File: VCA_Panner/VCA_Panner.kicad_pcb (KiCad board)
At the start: 2 copper layers, 43 x 110 mm, 70 parts, among them J1 CV1, J2 CV2, J3 Ch1_in, J4 Ch1_out, J6 Ch2_in, J7 Ch2_out, U1 TL074, U2 TL074, U3 TL074, U5 AS3360

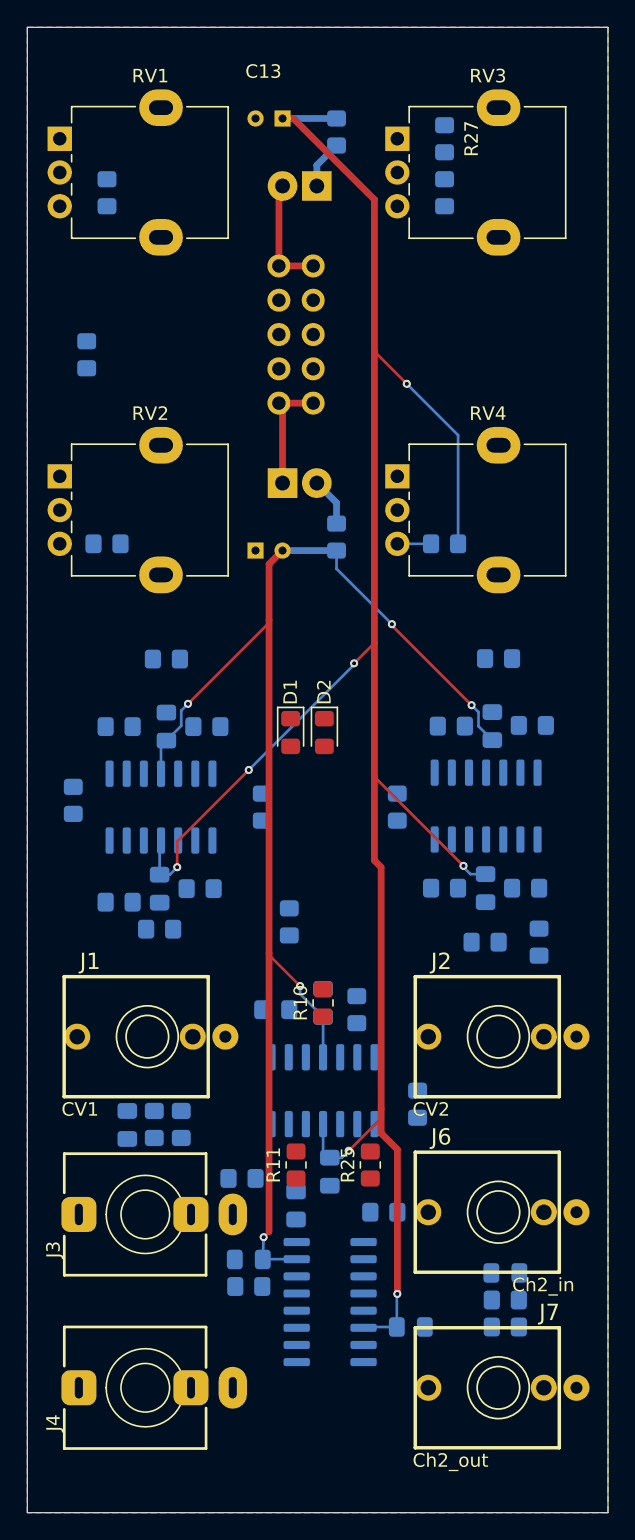
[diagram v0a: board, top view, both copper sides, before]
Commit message: vca_panner led added, routing started
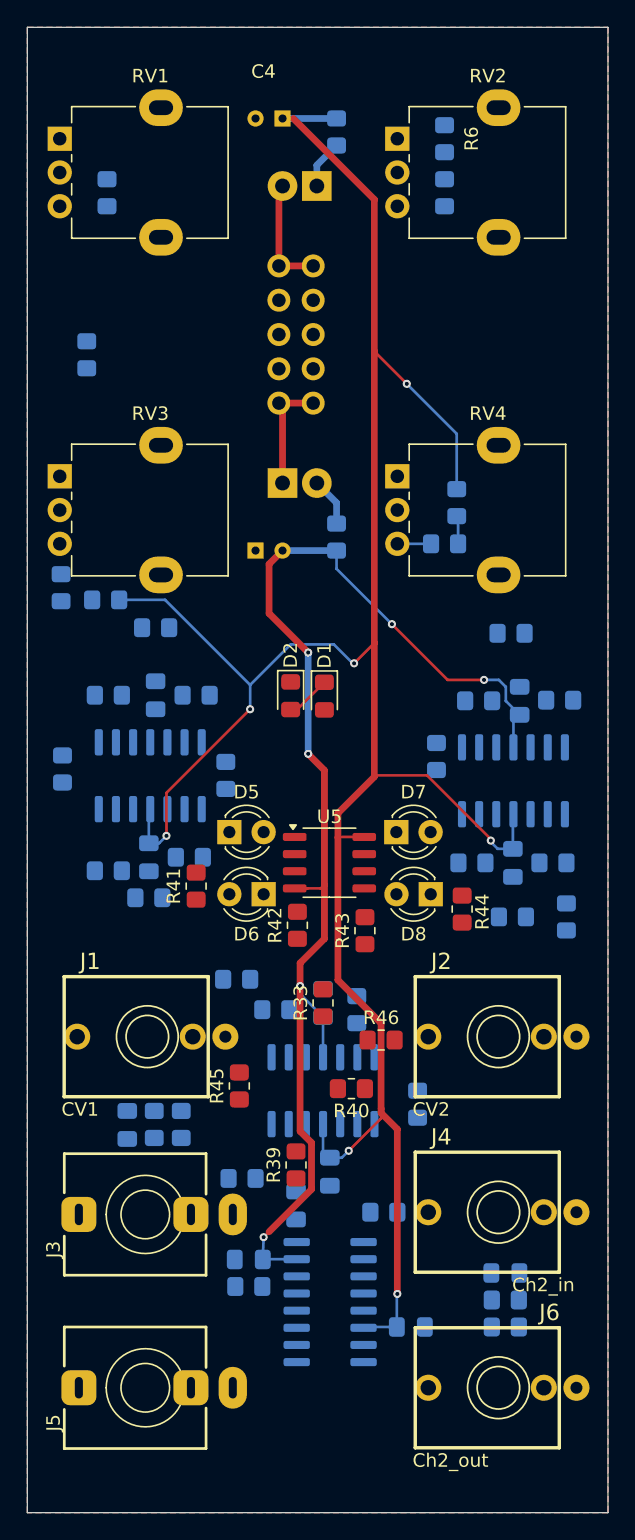
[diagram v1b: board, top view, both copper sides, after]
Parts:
- removed the R14 at (113.0, 95.5)
- added D5: LED, LED_THT:LED_D3.0mm, F.Cu at (122.1, 116.8)
- added D6: LED, LED_THT:LED_D3.0mm, F.Cu at (124.6, 121.5)
- added D7: LED, LED_THT:LED_D3.0mm, F.Cu at (134.4, 116.8)
- added D8: LED, LED_THT:LED_D3.0mm, F.Cu at (137.0, 121.5)
- added R23: 330k, Resistor_SMD:R_0805_2012Metric_Pad1.20x1.40mm_HandSolder, B.Cu at (109.6, 98.8)
- added R24: 400k, Resistor_SMD:R_0805_2012Metric_Pad1.20x1.40mm_HandSolder, B.Cu at (112.9, 99.7)
- added R26: 400k, Resistor_SMD:R_0805_2012Metric_Pad1.20x1.40mm_HandSolder, B.Cu at (138.9, 92.5)
- added R41: 1M, Resistor_SMD:R_0805_2012Metric_Pad1.20x1.40mm_HandSolder, F.Cu at (119.6, 120.8)
- added R42: 1.5k, Resistor_SMD:R_0805_2012Metric_Pad1.20x1.40mm_HandSolder, F.Cu at (127.1, 123.8)
- added R43: 1M, Resistor_SMD:R_0805_2012Metric_Pad1.20x1.40mm_HandSolder, F.Cu at (132.1, 124.2)
- added R44: 1.5k, Resistor_SMD:R_0805_2012Metric_Pad1.20x1.40mm_HandSolder, F.Cu at (139.3, 122.5)
- added R45: 1M, Resistor_SMD:R_0805_2012Metric_Pad1.20x1.40mm_HandSolder, F.Cu at (122.8, 135.7)
- added R46: 1M, Resistor_SMD:R_0805_2012Metric_Pad1.20x1.40mm_HandSolder, F.Cu at (133.3, 132.2)
- added U5: LM358, Package_SO:SO-8_3.9x4.9mm_P1.27mm, F.Cu at (129.5, 119.1)
- R25: renamed from R28; value 730k -> 330k
- moved R40 5.82 mm to (131.1, 135.8), turned to 180 degrees
- moved R34 5.77 mm to (122.6, 127.8), turned to 180 degrees
- moved R22 4.74 mm to (137.4, 111.2)
- moved R4 3.58 mm to (121.8, 112.7)
- moved C7 2.76 mm to (143.6, 107.1)
- moved C8 2.76 mm to (143.1, 119.1)
- moved R10 2.76 mm to (147.0, 123.1)
- moved R12 2.76 mm to (146.0, 119.1)
- moved R16 2.76 mm to (143.0, 123.1)
- moved R20 2.76 mm to (140.0, 119.1)
- moved R28 2.76 mm to (140.5, 107.1)
- moved R32 2.76 mm to (146.5, 107.1)
- moved U4 2.76 mm to (143.1, 113.0)
- moved D2 2.72 mm to (126.6, 106.8)
- moved D1 2.70 mm to (129.1, 106.8)
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- renumbered C5 to C1, C3 to C10, C9 to C11, C10 to C12, C4 to C13, C6 to C2, C11 to C3, C13 to C4, C12 to C5, C1 to C6, C2 to C8, C8 to C9, D2 to D1, D1 to D2, J6 to J4, J4 to J5, J7 to J6, J5 to J7, R29 to R1, R20 to R10, R1 to R11, R15 to R12, R32 to R13, R36 to R14, R7 to R15, R21 to R16, R30 to R17, R34 to R18, R2 to R19, R33 to R2, R16 to R20, R8 to R21, R3 to R27, R17 to R28, R9 to R29, R12 to R3, R23 to R30, R4 to R31, R18 to R32, R10 to R33, R24 to R34, R37 to R35, R38 to R36, R5 to R37, R19 to R38, R11 to R39, R13 to R4, R25 to R40, R26 to R5, R27 to R6, R31 to R7, R35 to R8, R6 to R9, RV3 to RV2, RV2 to RV3, U5 to U1, U1 to U3, U3 to U4
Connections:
- R25 pad 2: +12V -> Net-(R25-Pad2)
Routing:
- net +12V: track 163.7 -> 182.8 mm
- net -12V: track 102.6 -> 96.1 mm, vias 5 -> 6
- net Net-(D1-K): track 0.00 -> 3.34 mm
- net Net-(R25-Pad2): track 0.00 -> 2.09 mm

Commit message: pcb done, next panel
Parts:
- removed D5, D7: LED, LED_THT:LED_D3.0mm
- moved J5 1.18 mm to (117.0, 158.0)
- moved J3 1.16 mm to (117.0, 145.0)
- moved J1 0.99 mm to (117.0, 132.0)
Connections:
- J4 pad TN: audio_from_ch1 -> audio_to_ch2
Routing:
- net CV2: track 0.00 -> 98.6 mm, vias 0 -> 2
- net Net-(U3A-+): track 0.00 -> 60.0 mm, vias 0 -> 1
- net Net-(U4A-+): track 0.00 -> 58.7 mm
- net CV1: track 0.00 -> 47.5 mm, vias 0 -> 1
- net Net-(U3A--): track 0.00 -> 45.3 mm, vias 0 -> 4
- net Net-(R32-Pad1): track 0.00 -> 41.2 mm, vias 0 -> 2
- net audio_to_ch2: track 0.00 -> 38.8 mm
- net GND: track 0.00 -> 37.5 mm, vias 0 -> 57
- net audio_from_ch2: track 0.00 -> 36.0 mm
- net Net-(D1-A): track 0.00 -> 31.3 mm, vias 0 -> 2
- net Net-(D1-K): track 3.34 -> 33.8 mm, vias 0 -> 1
- net Net-(U1B-IO2): track 0.00 -> 29.5 mm
- net Net-(R31-Pad1): track 0.00 -> 26.9 mm, vias 0 -> 1
- net Net-(C3-Pad2): track 0.00 -> 26.9 mm, vias 0 -> 2
- net Net-(U5A-+): track 0.00 -> 24.7 mm
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
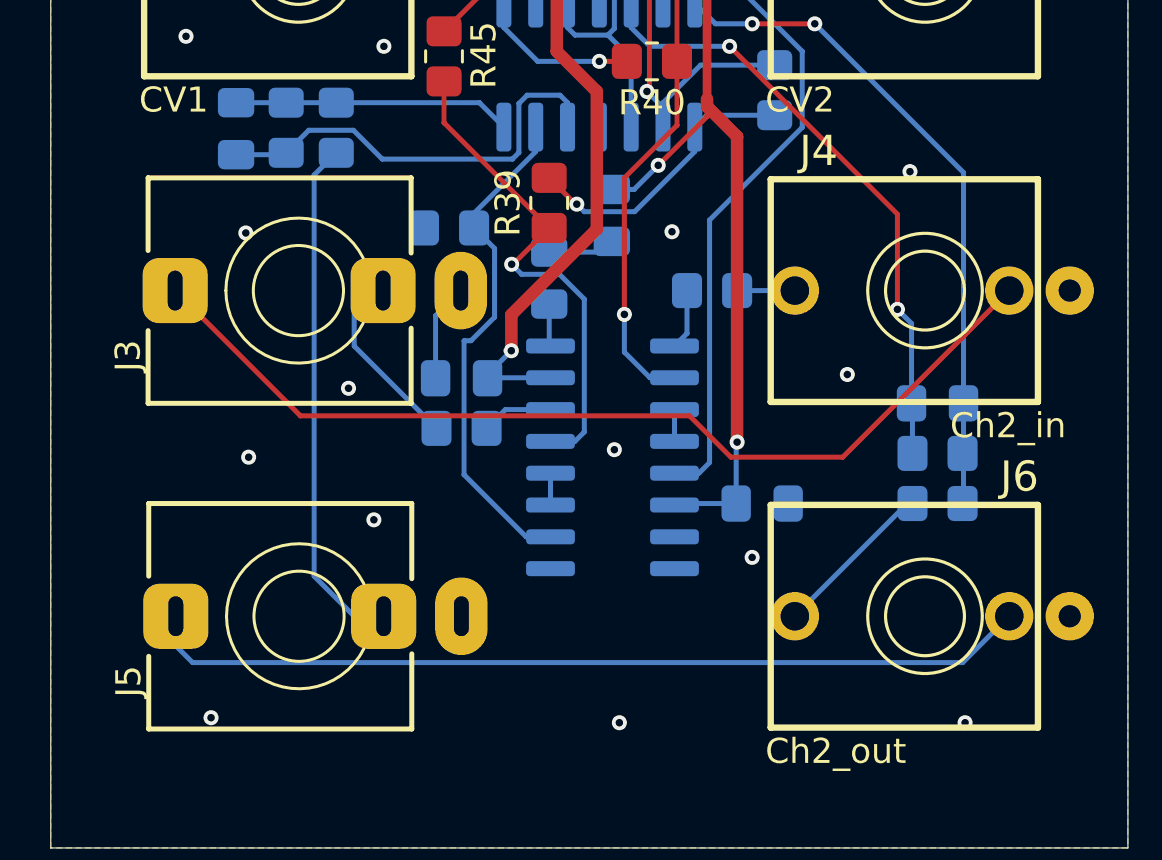
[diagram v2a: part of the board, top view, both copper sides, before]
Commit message: vca panner
All done, first set ordered
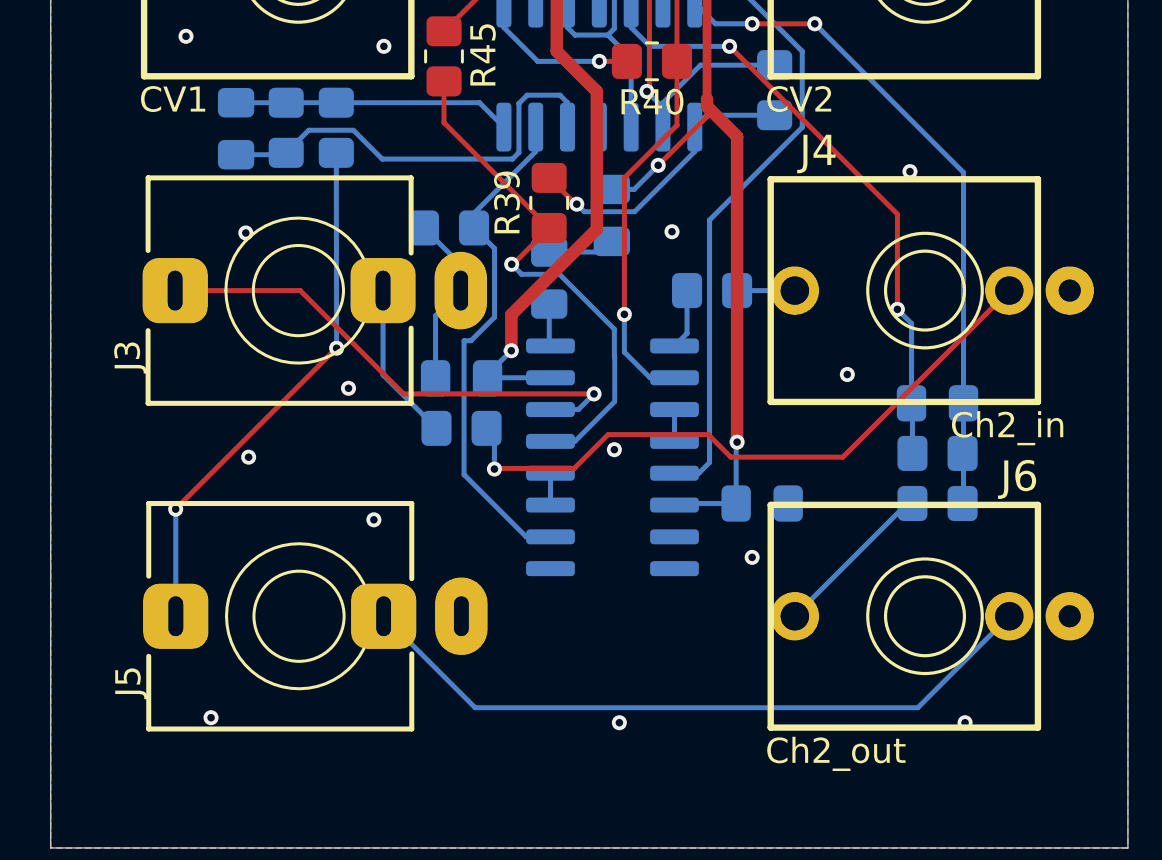
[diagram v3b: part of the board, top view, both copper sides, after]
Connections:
- J3 pad T: audio_to_ch2 -> audio1_to_vca1
- J5 pad R: Net-(J5-PadR) -> audio_from_ch2
- J5 pad T: audio_from_ch2 -> Net-(J5-PadT)
- R1 pad 2: audio1_to_vca1 -> audio_to_ch2
- R17 pad 2: Net-(J5-PadR) -> Net-(J5-PadT)
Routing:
- net Net-(J5-PadT): track 0.00 -> 21.2 mm, vias 0 -> 2
- net Net-(J5-PadR): track 19.5 -> 0.00 mm
- net audio1_to_vca1: track 2.86 -> 21.3 mm, vias 0 -> 1
- net audio_to_ch2: track 38.8 -> 25.7 mm, vias 0 -> 1
- net audio_from_ch2: track 36.0 -> 28.0 mm
- net GND: track 37.5 -> 40.1 mm
- net cv1_to_vca1: track 20.0 -> 21.0 mm
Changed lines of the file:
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@@
 		(grid_origin 141.9873 158)
 		(pcbplotparams
-			(layerselection 0x00010fc_ffffffff)
+			(layerselection 0x00010f0_ffffffff)
 			(plot_on_all_layers_selection 0x0000000_00000000)
 			(disableapertmacros no)
@@
 			(outputformat 1)
 			(mirror no)
-			(drillshape 1)
+			(drillshape 0)
 			(scaleselection 1)
-			(outputdirectory "")
+			(outputdirectory "vca_gerber/")
 		)
 	)
@@
 	(net 24 "Net-(D8-K)")
 	(net 25 "Net-(J4-PadT)")
-	(net 26 "Net-(J5-PadR)")
+	(net 26 "Net-(J5-PadT)")
 	(net 27 "Net-(U4A-+)")
 	(net 28 "Net-(U1A-IO1)")
@@
 			(remove_unused_layers no)
 			(roundrect_rratio 0.25)
-			(net 26 "Net-(J5-PadR)")
+			(net 20 "audio_from_ch2")
 			(pintype "passive")
 		)
@@
 			(remove_unused_layers no)
 			(roundrect_rratio 0.25)
-			(net 20 "audio_from_ch2")
+			(net 26 "Net-(J5-PadT)")
 			(pintype "passive")
 		)
@@
 			(remove_unused_layers no)
 			(roundrect_rratio 0.25)
-			(net 17 "audio_to_ch2")
+			(net 48 "audio1_to_vca1")
 			(pintype "passive")
 		)
@@
 			(layers "B.Cu" "B.Paste" "B.Mask")
 			(roundrect_rratio 0.208333)
-			(net 26 "Net-(J5-PadR)")
+			(net 26 "Net-(J5-PadT)")
 			(pintype "passive")
 		)
@@
 			(layers "B.Cu" "B.Paste" "B.Mask")
 			(roundrect_rratio 0.208333)
-			(net 48 "audio1_to_vca1")
+			(net 17 "audio_to_ch2")
 			(pintype "passive")
 		)
@@
 	)
 	(segment
+		(start 123.4673 145)
+		(end 123.4673 143.9673)
+		(width 0.2)
+		(layer "B.Cu")
+		(net 1)
+	)
+	(segment
 		(start 115.3 104.375)
 		(end 115.3 103.25)
@@
 	)
 	(segment
-		(start 122.315 142.815)
+		(start 123.4673 143.9673)
 		(end 122 142.5)
 		(width 0.2)
@@
 	)
 	(segment
-		(start 132.601471 150)
+		(start 138.7155 151.65)
 		(end 134.251471 151.65)
 		(width 0.2)
@@
 	)
 	(segment
-		(start 117.0673 150)
-		(end 132.601471 150)
+		(start 129.351471 150.75)
+		(end 128.001471 152.1)
 		(width 0.2)
 		(layer "F.Cu")
@@
 	)
 	(segment
-		(start 112.0673 145)
-		(end 117.0673 150)
+		(start 124.8123 152.125)
+		(end 124.7873 152.125)
 		(width 0.2)
 		(layer "F.Cu")
@@
 	)
 	(segment
-		(start 138.7155 151.65)
-		(end 145.3655 145)
+		(start 134.251471 151.65)
+		(end 133.351471 150.75)
 		(width 0.2)
 		(layer "F.Cu")
@@
 	)
 	(segment
-		(start 134.251471 151.65)
+		(start 128.001471 152.1)
+		(end 124.8123 152.1)
+		(width 0.2)
+		(layer "F.Cu")
+		(net 17)
+	)
+	(segment
+		(start 145.3655 145)
 		(end 138.7155 151.65)
 		(width 0.2)
@@
 	)
 	(segment
-		(start 119.215 147.215)
-		(end 119.215 145.165)
+		(start 124.7873 152.125)
+		(end 124.8123 152.1)
+		(width 0.2)
+		(layer "F.Cu")
+		(net 17)
+	)
+	(segment
+		(start 124.8123 152.1)
+		(end 124.8123 152.125)
+		(width 0.2)
+		(layer "F.Cu")
+		(net 17)
+	)
+	(segment
+		(start 133.351471 150.75)
+		(end 129.351471 150.75)
+		(width 0.2)
+		(layer "F.Cu")
+		(net 17)
+	)
+	(via
+		(at 124.8123 152.125)
+		(size 0.6)
+		(drill 0.3)
+		(layers "F.Cu" "B.Cu")
+		(net 17)
+	)
+	(segment
+		(start 124.8123 150.8123)
+		(end 124.782843 150.782843)
+		(width 0.2)
+		(layer "B.Cu")
+		(net 17)
+	)
+	(segment
+		(start 124.8123 152.125)
+		(end 124.8123 150.8123)
+		(width 0.2)
+		(layer "B.Cu")
+		(net 17)
+	)
+	(segment
+		(start 120.3673 148.3673)
+		(end 122.5 150.5)
 		(width 0.2)
 		(layer "B.Cu")
@@
 	)
 	(segment
-		(start 122.5 150.5)
-		(end 119.215 147.215)
+		(start 120.3673 145)
+		(end 120.3673 148.3673)
 		(width 0.2)
 		(layer "B.Cu")
@@
 	)
 	(segment
-		(start 110.915 158)
-		(end 112.765 159.85)
+		(start 141.7155 161.65)
+		(end 124.0427 161.65)
 		(width 0.2)
 		(layer "B.Cu")
@@
 	)
 	(segment
-		(start 143.5028 159.85)
-		(end 145.3528 158)
+		(start 124.0427 161.65)
+		(end 120.3927 158)
 		(width 0.2)
 		(layer "B.Cu")
@@
 	)
 	(segment
-		(start 112.765 159.85)
-		(end 143.5028 159.85)
+		(start 145.3655 158)
+		(end 141.7155 161.65)
 		(width 0.2)
 		(layer "B.Cu")
@@
 	(segment
 		(start 134.5 145)
-		(end 136.793 145)
+		(end 136.8057 145)
 		(width 0.2)
 		(layer "B.Cu")
@@
 	)
 	(segment
+		(start 118.501471 147.3)
+		(end 118.5123 147.3)
+		(width 0.2)
+		(layer "F.Cu")
+		(net 26)
+	)
+	(segment
+		(start 112.0873 153.725)
+		(end 112.0873 153.714171)
+		(width 0.2)
+		(layer "F.Cu")
+		(net 26)
+	)
+	(segment
+		(start 112.0873 153.714171)
+		(end 118.501471 147.3)
+		(width 0.2)
+		(layer "F.Cu")
+		(net 26)
+	)
+	(via
+		(at 112.0873 153.725)
+		(size 0.6)
+		(drill 0.3)
+		(layers "F.Cu" "B.Cu")
+		(net 26)
+	)
+	(via
+		(at 118.5123 147.3)
+		(size 0.6)
+		(drill 0.3)
+		(layers "F.Cu" "B.Cu")
+		(net 26)
+	)
+	(segment
 		(start 118.5 139.5)
-		(end 117.615 140.385)
+		(end 118.5123 147.3)
+		(width 0.2)
+		(layer "B.Cu")
+		(net 26)
+	)
+	(segment
+		(start 112.0927 153.7196)
+		(end 112.0873 153.725)
+		(width 0.2)
+		(layer "B.Cu")
+		(net 26)
+	)
+	(segment
+		(start 112.0873 153.725)
+		(end 112.0927 153.7304)
 		(width 0.2)
 		(layer "B.Cu")
@@
 	)
 	(segment
-		(start 117.615 140.385)
-		(end 117.615 156.4)
+		(start 112.0927 153.708771)
+		(end 112.0927 153.7196)
 		(width 0.2)
 		(layer "B.Cu")
@@
 	)
 	(segment
-		(start 117.615 156.4)
-		(end 119.215 158)
+		(start 112.0927 153.7304)
+		(end 112.0927 158)
+		(width 0.2)
+		(layer "B.Cu")
+		(net 26)
+	)
+	(segment
+		(start 118.5123 147.3)
+		(end 118.5 147.301471)
 		(width 0.2)
 		(layer "B.Cu")
@@
 	)
 	(segment
+		(start 129.6 146.540256)
+		(end 127.409744 144.35)
+		(width 0.2)
+		(layer "B.Cu")
+		(net 33)
+	)
+	(segment
 		(start 128.024999 151.02)
-		(end 128.4 150.644999)
+		(end 129.6123 149.432699)
 		(width 0.2)
 		(layer "B.Cu")
@@
 	)
 	(segment
-		(start 128.4 145.340256)
-		(end 127.409744 144.35)
+		(start 129.6 147.620685)
+		(end 129.6 146.540256)
 		(width 0.2)
 		(layer "B.Cu")
@@
 	)
 	(segment
-		(start 128.4 150.644999)
-		(end 128.4 145.340256)
+		(start 125.9 144.35)
+		(end 125.5 143.95)
+		(width 0.2)
+		(layer "B.Cu")
+		(net 33)
+	)
+	(segment
+		(start 129.6123 147.632985)
+		(end 129.6 147.620685)
 		(width 0.2)
 		(layer "B.Cu")
@@
 	)
 	(segment
-		(start 125.9 144.35)
-		(end 125.5 143.95)
+		(start 129.6123 149.432699)
+		(end 129.6123 147.632985)
 		(width 0.2)
 		(layer "B.Cu")
@@
 	)
 	(segment
-		(start 124.5 150.5)
-		(end 125.25 149.75)
+		(start 128.7873 149.125)
+		(end 121.185829 149.125)
+		(width 0.2)
+		(layer "F.Cu")
+		(net 48)
+	)
+	(segment
+		(start 117.060829 145)
+		(end 112.0673 145)
+		(width 0.2)
+		(layer "F.Cu")
+		(net 48)
+	)
+	(segment
+		(start 121.185829 149.125)
+		(end 117.060829 145)
+		(width 0.2)
+		(layer "F.Cu")
+		(net 48)
+	)
+	(via
+		(at 128.7873 149.125)
+		(size 0.6)
+		(drill 0.3)
+		(layers "F.Cu" "B.Cu")
+		(net 48)
+	)
+	(segment
+		(start 112.0673 145)
+		(end 112.4623 145)
+		(width 0.2)
+		(layer "B.Cu")
+		(net 48)
+	)
+	(segment
+		(start 127.05 149.75)
+		(end 128.1623 149.75)
+		(width 0.2)
+		(layer "B.Cu")
+		(net 48)
+	)
+	(segment
+		(start 128.1623 149.75)
+		(end 128.7873 149.125)
 		(width 0.2)
 		(layer "B.Cu")
@@
 	)
 	(segment
-		(start 125.25 149.75)
-		(end 127.05 149.75)
+		(start 112.4623 145)
+		(end 112.8123 145.35)
 		(width 0.2)
 		(layer "B.Cu")
